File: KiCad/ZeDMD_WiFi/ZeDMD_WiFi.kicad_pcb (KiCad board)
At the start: 4 copper layers, 100 x 80 mm, 25 parts, among them J1 max98357-L, J10 Conn_01x02_Pin, J11 Conn_01x02_Pin, J2 MicroSD, J3 max98357-R, J4 MAX_Vin_SELECT, J5 RGBout_SELECT, J6 5Vin_OPTION, J7 KF7.62 Barrier Terminal Block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, J8 USB-C breakout, J9 Conn_02x08_Odd_Even, SW1 Menu Left, SW2 Boot/Value+, SW3 Value-, SW4 Menu Right, U1 ESP32-S3-DevKitC

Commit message: change DevKit row spacing
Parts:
- moved J7 4.74 mm to (221.7, 142.0)
- moved J6 4.53 mm to (225.3, 132.8)
- moved U1 2.54 mm to (150.5, 135.3)
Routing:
- net /ESP32-S3-DevKitC-1-N16R8/ESP5V: track 154.0 -> 160.0 mm
- net /ZeDMD/HUB_B: track 10.9 -> 16.4 mm
- net /RGBout_5Vin: track 20.3 -> 15.6 mm
- net GND: track 11.7 -> 15.2 mm
- net +3.3V: track 69.7 -> 72.4 mm
- net /LRC: track 78.3 -> 80.9 mm
- net /ZeDMD/HUB_G1: track 8.78 -> 6.24 mm
- net /ZeDMD/HUB_R2: track 11.3 -> 8.78 mm
- net /ZeDMD/HUB_R1: track 14.2 -> 11.7 mm
- net /ZeDMD/HUB_B2: track 12.4 -> 9.83 mm
- net /ZeDMD/HUB_B1: track 11.3 -> 8.78 mm
- net /ZeDMD/HUB_A: track 12.4 -> 9.83 mm
- net /SCK: track 47.4 -> 49.9 mm
- net /MOSI: track 51.0 -> 53.6 mm
- net /MISO: track 52.9 -> 55.4 mm
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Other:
- board text added: "3V3"
- board text added: "Rev: 1.2"
- board text removed: "Rev: 1.1"

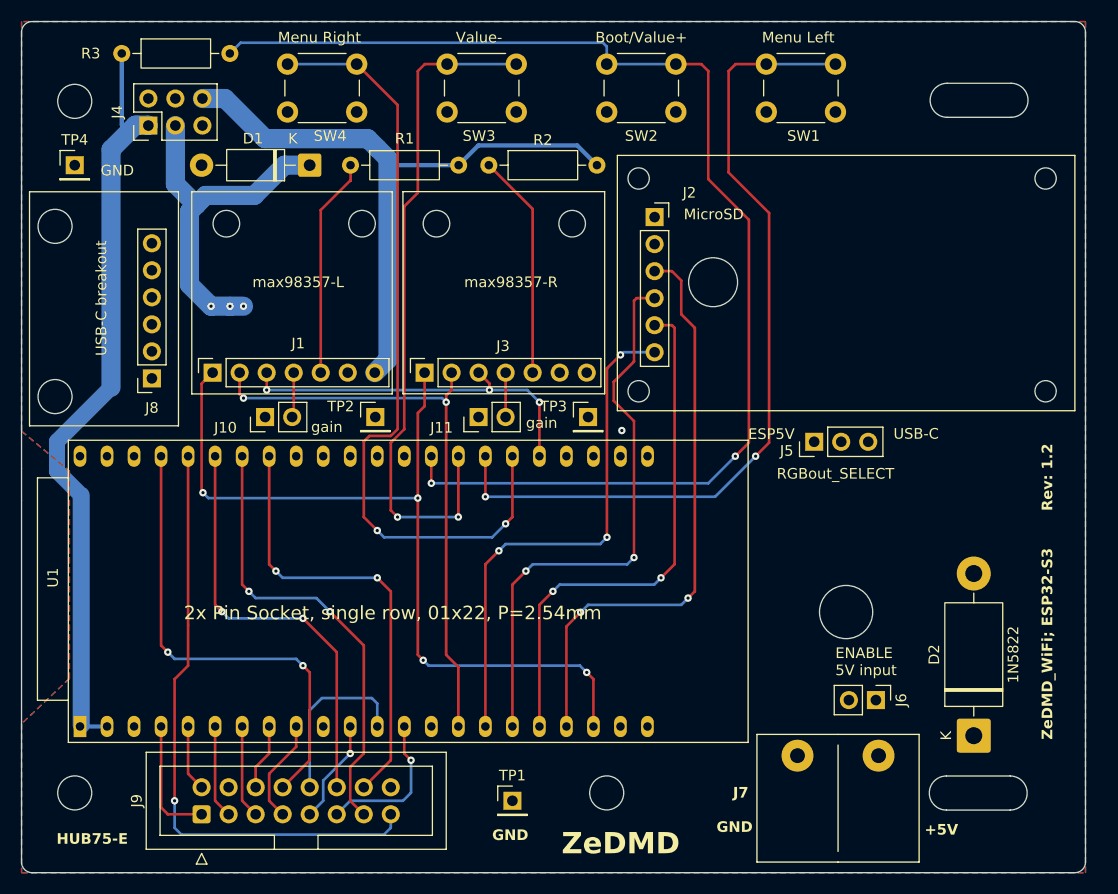
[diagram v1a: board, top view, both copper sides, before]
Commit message: Update PCB to Rev1.3
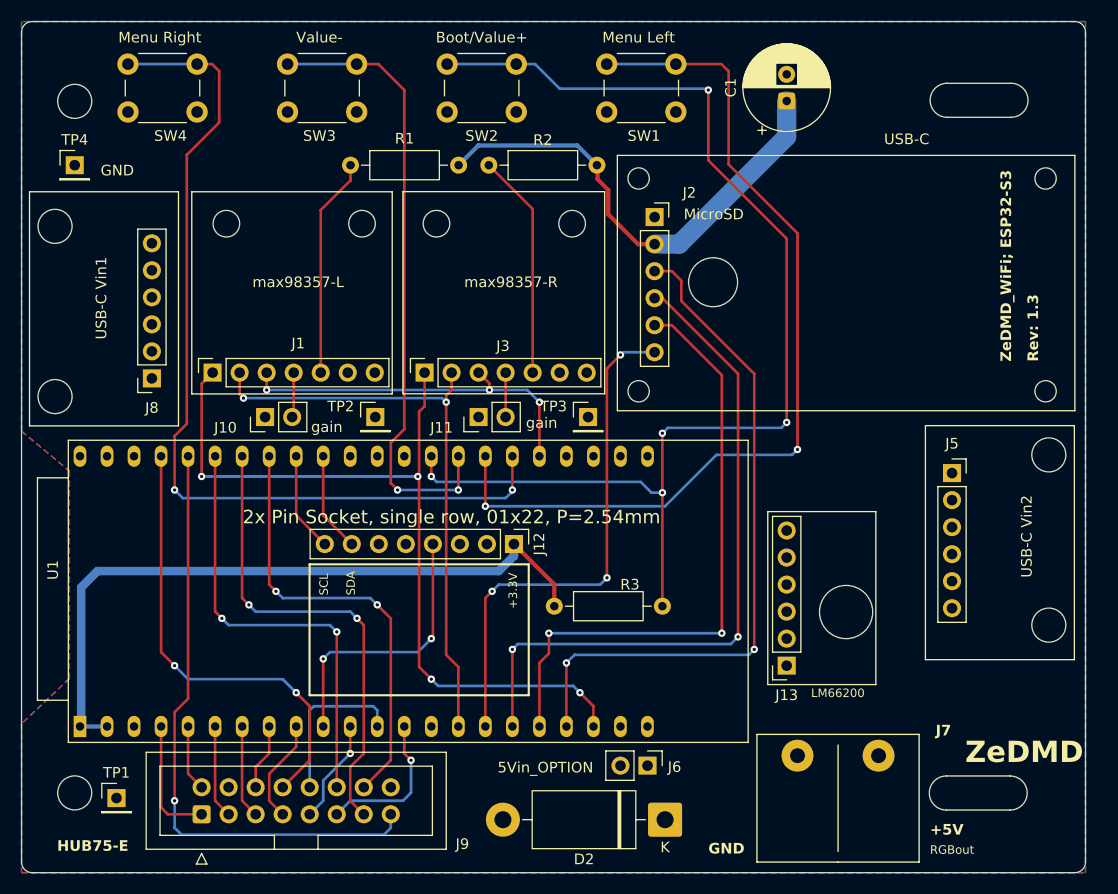
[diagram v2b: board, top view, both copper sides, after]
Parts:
- removed D1: 1N5819, Diode_THT:D_DO-41_SOD81_P10.16mm_Horizontal
- removed J4: MAX_Vin_SELECT, Connector_PinHeader_2.54mm:PinHeader_2x03_P2.54mm_Vertical
- added C1: 100uF/16V, Capacitor_THT:CP_Radial_D8.0mm_P2.50mm, F.Cu at (216.9, 76.5)
- added J12: ADXL345, Connector_PinHeader_2.54mm:PinHeader_1x08_P2.54mm_Vertical, F.Cu at (191.3, 118.1)
- added J13: LM66200, Connector_PinSocket_2.54mm:PinSocket_1x06_P2.54mm_Vertical, F.Cu at (216.9, 129.5)
- J5: value RGBout_SELECT -> USB-C Vin2; footprint Connector_PinHeader_2.54mm:PinHeader_1x03_P2.54mm_Vertical -> Connector_PinSocket_2.54mm:PinSocket_1x06_P2.54mm_Vertical
- J8: value USB-C breakout -> USB-C Vin1
- moved R3 66.0 mm to (195.1, 124.0)
- moved TP1 37.2 mm to (153.9, 142.0)
- moved D2 30.1 mm to (205.5, 144.0), turned to 180 degrees
- moved J6 22.3 mm to (203.8, 138.9)
- moved SW1 15.0 mm to (200.0, 73.0)
- moved SW2 15.0 mm to (185.0, 73.0)
- moved SW3 15.0 mm to (170.0, 73.0)
- moved SW4 15.0 mm to (155.0, 73.0)
- moved J5 13.3 mm to (232.5, 111.4), turned to 0 degrees
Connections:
- D2 pad 2: /RGBout -> /ESP32-S3-DevKitC-1-N16R8/ESP5V
- J1 pad 7: /MAX_Vin -> /ESP32-S3-DevKitC-1-N16R8/ESP5V
- J3 pad 7: /MAX_Vin -> /ESP32-S3-DevKitC-1-N16R8/ESP5V
- J5 pad 1: /ESP32-S3-DevKitC-1-N16R8/ESP5V -> unconnected-(J5-Pin_1-Pad1)
- J5 pad 2: /RGBout -> unconnected-(J5-Pin_2-Pad2)
- J5 pad 3: /VBUS -> unconnected-(J5-Pin_3-Pad3)
- J8 pad 6: /VBUS -> /VBUS1
- R1 pad 2: /MAX_Vin -> /ESP32-S3-DevKitC-1-N16R8/ESP5V
- R2 pad 2: /MAX_Vin -> /ESP32-S3-DevKitC-1-N16R8/ESP5V
- TP2 pad 1: /MAX_Vin -> /ESP32-S3-DevKitC-1-N16R8/ESP5V
- TP3 pad 1: /MAX_Vin -> /ESP32-S3-DevKitC-1-N16R8/ESP5V
- U1 pad 10: unconnected-(U1-GPIO17/ADC2_CH6-Pad10) -> /INT1
- U1 pad 35: unconnected-(U1-GPIO38-Pad35) -> /I2C_SDA
- U1 pad 36: unconnected-(U1-GPIO39/MTCK-Pad36) -> /I2C_SCL
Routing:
- net /VBUS: track 117.6 -> 0.00 mm
- net /VBUS1: track 0.00 -> 102.7 mm
- net /MAX_Vin: track 100.8 -> 0.00 mm
- net /INT1: track 0.00 -> 26.3 mm, vias 0 -> 2
- net /ESP32-S3-DevKitC-1-N16R8/ESP5V: track 160.0 -> 185.9 mm, vias 3 -> 0
- net /RGBout: track 22.6 -> 0.00 mm
- net /VBUS2: track 0.00 -> 17.6 mm
- net /RGBout_5Vin: track 15.6 -> 28.7 mm
- net /ZeDMD/BTN_RIGHT: track 74.4 -> 85.7 mm
- net /MOSI: track 53.6 -> 64.5 mm
- net /I2C_SDA: track 0.00 -> 9.37 mm
- net /I2C_SCL: track 0.00 -> 9.37 mm
- net /MISO: track 55.4 -> 64.5 mm
- net /SCK: track 49.9 -> 57.9 mm
- net /ZeDMD/BTN_LEFT: track 79.4 -> 86.8 mm
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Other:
- outline, holes or cut-outs redrawn
- board text added: "+3.3V"
- board text added: "5Vin_OPTION"
- board text added: "LM66200"
- board text added: "RGBout"
- board text added: "Rev: 1.3"
- board text added: "SCL"
- board text added: "SDA"
- board text added: "USB-C Vin2"
- board text added: "VBUS1:5V"
- board text added: "VBUS2:5V"
- board text added: "https://github.com/jens-b/The-Arcade"
- board text removed: "3V3"
- board text removed: "ENABLE 5V input"
- board text removed: "ESP5V"
- board text removed: "Rev: 1.2"
- board text removed: "VBUS 5V"
- board text removed: "https://github.com/jens-b/ZeDMD-5.1.8-WIFI-128x32"

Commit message: Fix J12 reversed power supply pins
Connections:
- J12 pad 1: +3.3V -> GND
- J12 pad 2: GND -> +3.3V
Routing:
- net +3.3V: track 65.9 -> 67.4 mm
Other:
- board text added: "Rev: 1.4"
- board text added: "VBUS1"
- board text added: "VBUS2"
- board text removed: "Rev: 1.3"
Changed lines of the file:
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@@
 	(title_block
 		(title "ZeDMD-WIFI-128x32")
-		(date "2026-09-04")
-		(rev "1.3")
+		(date "2026-09-19")
+		(rev "1.4")
 		(company "elabree")
 		(comment 1 "https://github.com/jens-b/ZeDMD-5.1.8-WIFI-128x32")
@@
 			(layers "*.Cu" "*.Mask")
 			(remove_unused_layers no)
-			(net "+3.3V")
+			(net "GND")
 			(pinfunction "Pin_1_1")
 			(pintype "passive")
@@
 			(layers "*.Cu" "*.Mask")
 			(remove_unused_layers no)
-			(net "GND")
+			(net "+3.3V")
 			(pinfunction "Pin_2_2")
 			(pintype "passive")
@@
 		(property "Value" "GND"
 			(at 0 2.38 0)
-			(layer "F.Fab")
+			(layer "B.SilkS")
 			(effects
 				(font
@@
 					(thickness 0.15)
 				)
+				(justify mirror)
 			)
 		)
@@
 		)
 	)
-	(gr_text "Rev: 1.3"
+	(gr_text "Rev: 1.4"
 		(at 240.665 100.965 90)
 		(layer "F.SilkS")
@@
 		)
 	)
+	(gr_text "VBUS2"
+		(at 222.504 120.015 0)
+		(layer "B.SilkS")
+		(effects
+			(font
+				(size 0.8 0.8)
+				(thickness 0.1)
+			)
+			(justify left bottom mirror)
+		)
+	)
+	(gr_text "VBUS1"
+		(at 222.631 117.475 0)
+		(layer "B.SilkS")
+		(effects
+			(font
+				(size 0.8 0.8)
+				(thickness 0.1)
+			)
+			(justify left bottom mirror)
+		)
+	)
 	(gr_text "14: LRC"
 		(at 163.322 95.25 90)
@@
 		)
 	)
+	(gr_text "GND"
+		(at 214.884 120.777 90)
+		(layer "B.SilkS")
+		(effects
+			(font
+				(size 0.8 0.8)
+				(thickness 0.1)
+			)
+			(justify left bottom mirror)
+		)
+	)
+	(gr_text "+5V"
+		(at 214.884 123.317 90)
+		(layer "B.SilkS")
+		(effects
+			(font
+				(size 0.8 0.8)
+				(thickness 0.1)
+			)
+			(justify left bottom mirror)
+		)
+	)
 	(gr_text "VBUS2:5V"
 		(at 234.061 123.698 180)
@@
 	)
 	(segment
-		(start 195.072 123.952)
-		(end 195.072 121.8992)
+		(start 195.072 121.8992)
+		(end 193.8228 120.65)
 		(width 0.4)
 		(layer "F.Cu")
@@
 	)
 	(segment
-		(start 195.072 121.8992)
-		(end 191.2828 118.11)
+		(start 189.611 120.65)
+		(end 188.7428 119.7818)
 		(width 0.4)
 		(layer "F.Cu")
@@
 	)
 	(segment
-		(start 191.2828 118.11)
-		(end 191.2828 119.2322)
-		(width 0.8)
-		(layer "B.Cu")
+		(start 193.8228 120.65)
+		(end 189.611 120.65)
+		(width 0.4)
+		(layer "F.Cu")
 		(net "+3.3V")
 	)
 	(segment
-		(start 152.146 120.65)
-		(end 150.60792 122.18808)
+		(start 195.072 123.952)
+		(end 195.072 121.8992)
+		(width 0.4)
+		(layer "F.Cu")
+		(net "+3.3V")
+	)
+	(segment
+		(start 188.7428 119.7818)
+		(end 188.7428 118.11)
+		(width 0.4)
+		(layer "F.Cu")
+		(net "+3.3V")
+	)
+	(segment
+		(start 150.60792 122.18808)
+		(end 150.60792 135.14208)
 		(width 0.8)
 		(layer "B.Cu")
@@
 	)
 	(segment
-		(start 189.865 120.65)
+		(start 188.7428 118.11)
+		(end 188.7428 120.1212)
+		(width 0.8)
+		(layer "B.Cu")
+		(net "+3.3V")
+	)
+	(segment
+		(start 188.214 120.65)
 		(end 152.146 120.65)
 		(width 0.8)
@@
 	)
 	(segment
-		(start 191.2828 119.2322)
-		(end 189.865 120.65)
+		(start 152.146 120.65)
+		(end 150.60792 122.18808)
 		(width 0.8)
 		(layer "B.Cu")
@@
 	)
 	(segment
-		(start 150.60792 122.18808)
-		(end 150.60792 135.14208)
+		(start 188.7428 120.1212)
+		(end 188.214 120.65)
 		(width 0.8)
 		(layer "B.Cu")
